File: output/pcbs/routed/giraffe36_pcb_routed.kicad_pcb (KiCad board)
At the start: 2 copper layers, 130.1 x 119 mm, 21 parts, among them U0 Pico

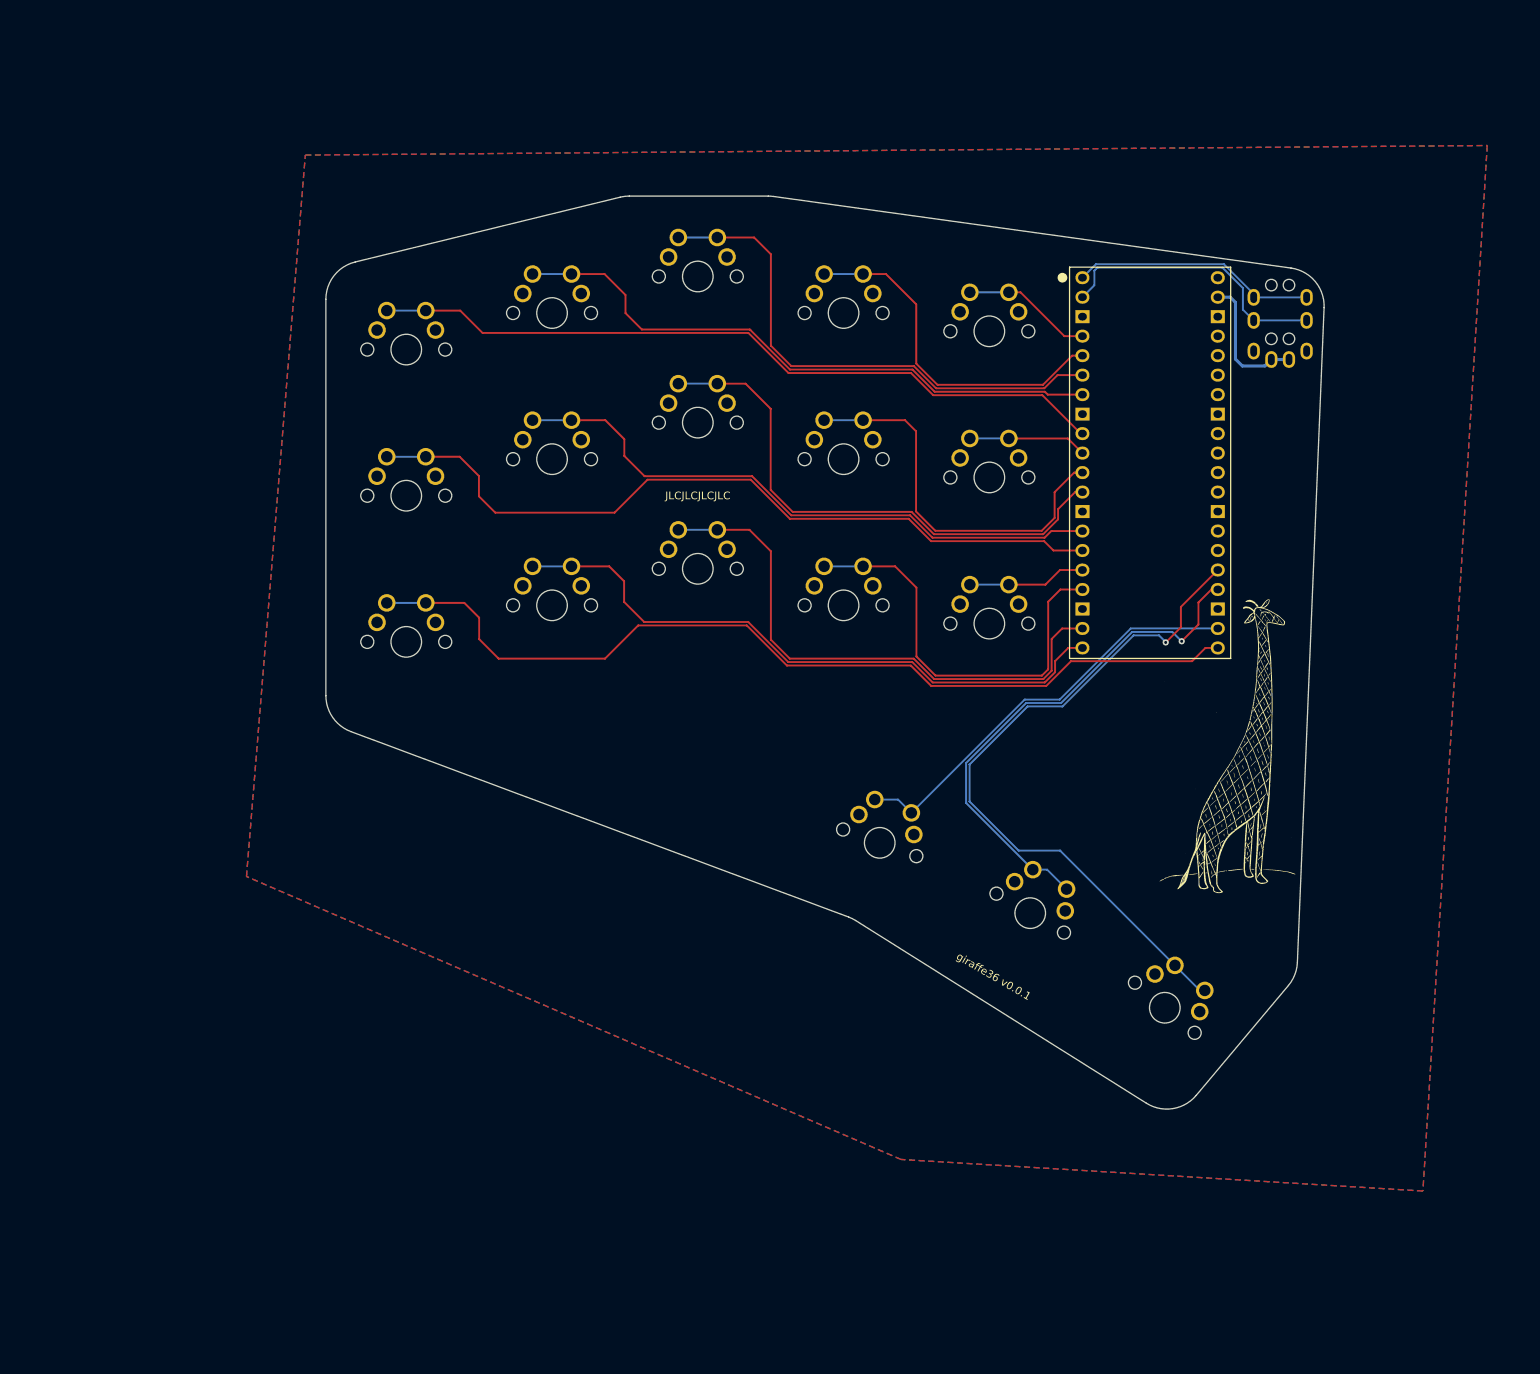
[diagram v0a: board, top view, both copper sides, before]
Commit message: give TRRS are more routing breathing room
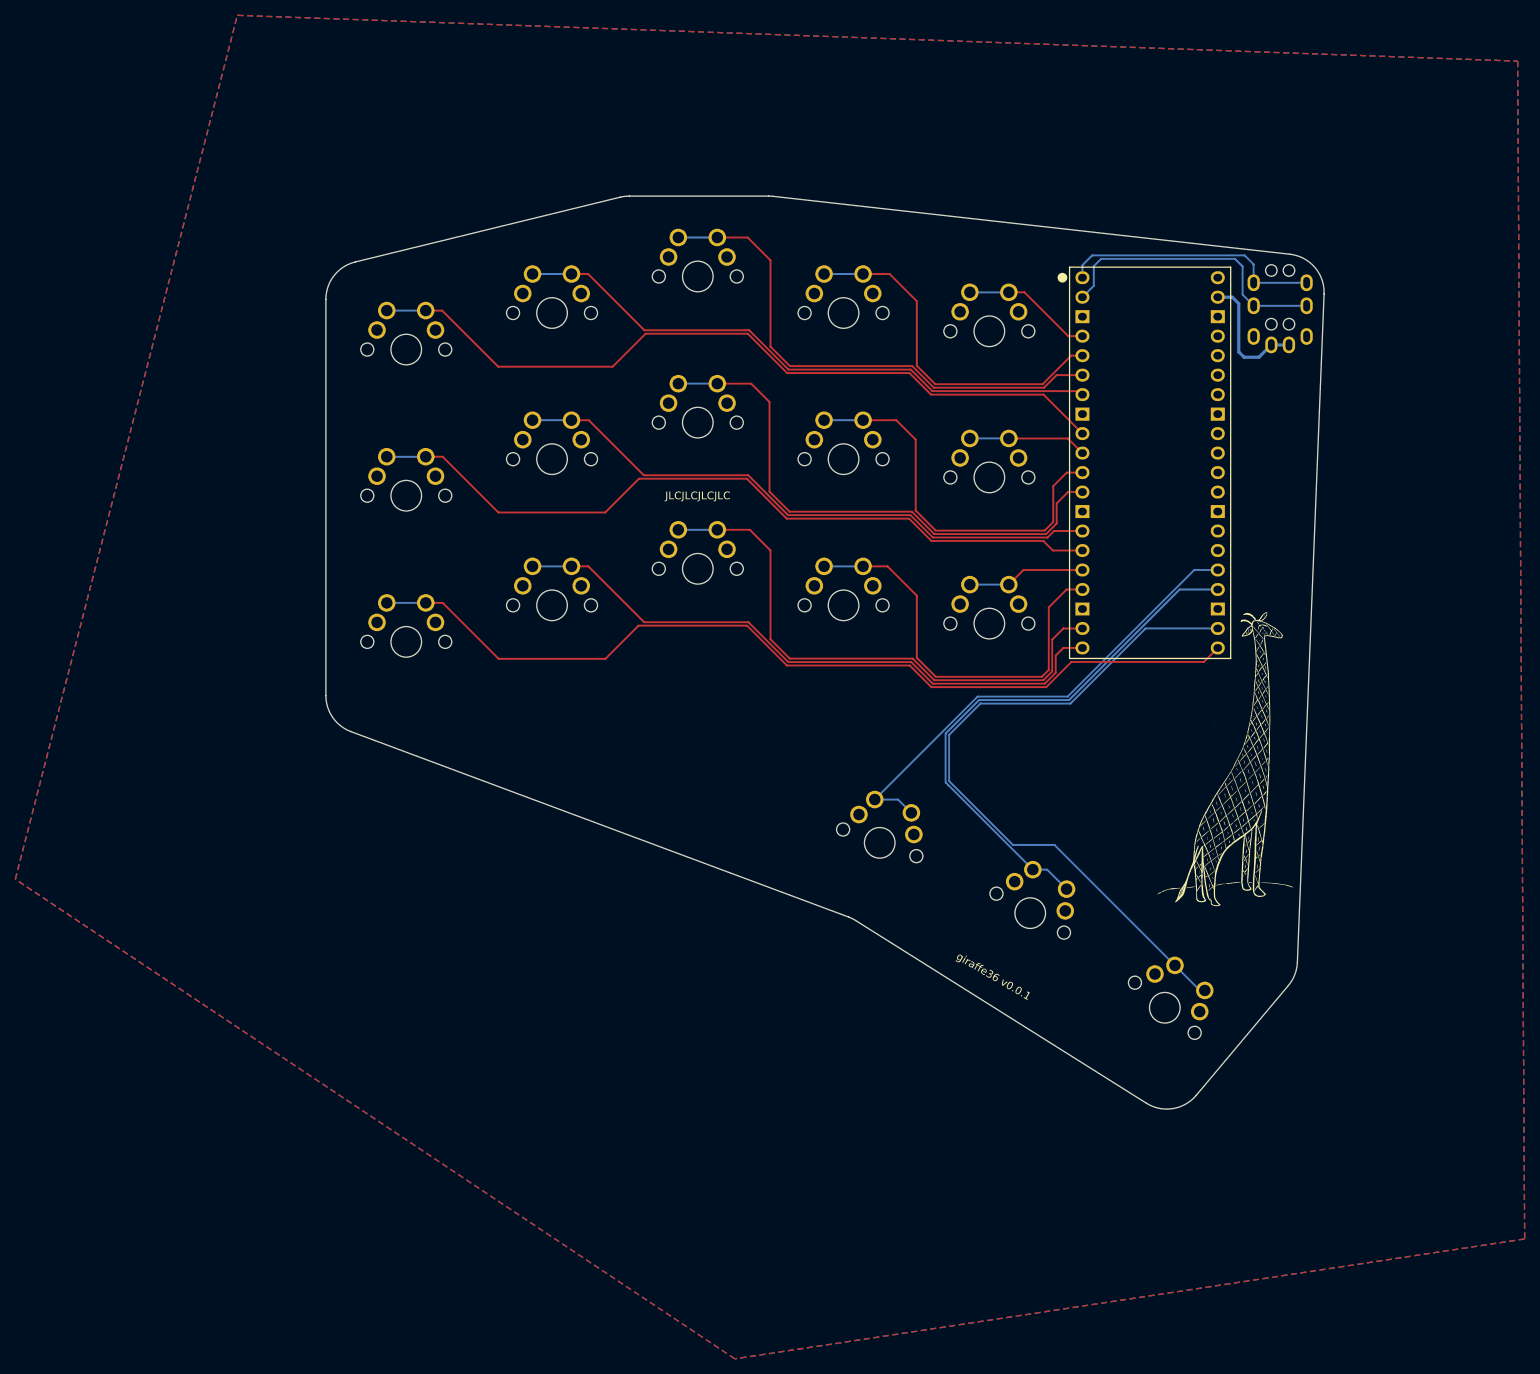
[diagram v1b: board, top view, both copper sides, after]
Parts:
- moved TRRS1 1.91 mm to (267.5, 102.4)
- moved G*** 1.73 mm to (259.1, 168.0)
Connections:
- U0 pad 22: thumbfan_near_home -> thumbfan_far_home
- U0 pad 25: thumbfan_far_home -> thumbfan_near_home
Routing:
- net thumbfan_near_home: track 55.4 -> 62.6 mm
- net matrix_pinky_top: track 97.1 -> 100.9 mm
- net thumbfan_home_home: track 67.8 -> 71.1 mm, vias 1 -> 0
- net GP0: track 31.6 -> 34.2 mm
- net matrix_pinky_bottom: track 120.1 -> 118.6 mm
- net matrix_pinky_home: track 100.8 -> 99.4 mm
- net matrix_middle_home: track 70.0 -> 71.4 mm
- net matrix_ring_top: track 79.6 -> 78.2 mm
- net matrix_ring_home: track 79.6 -> 78.4 mm
- net thumbfan_far_home: track 90.3 -> 91.4 mm, vias 1 -> 0
- net GP1: track 36.4 -> 37.5 mm
- net matrix_ring_bottom: track 82.2 -> 81.2 mm
- net VSYS: track 17.7 -> 16.9 mm
- net matrix_index_bottom: track 54.6 -> 53.9 mm
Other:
- outline, holes or cut-outs redrawn
